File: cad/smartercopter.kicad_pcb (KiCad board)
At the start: 2 copper layers, 37.7 x 16.8 mm, 74 parts, among them P1 CONN_5, P2 CONN_01X01, P3 CONN_01X01, P4 CONN_2, P5 CONN_01X01, P6 CONN_01X01, P7 CONN_01X01, Q1 SiA910EDJ, SW1 SW_PUSH_4, U1 CC2541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

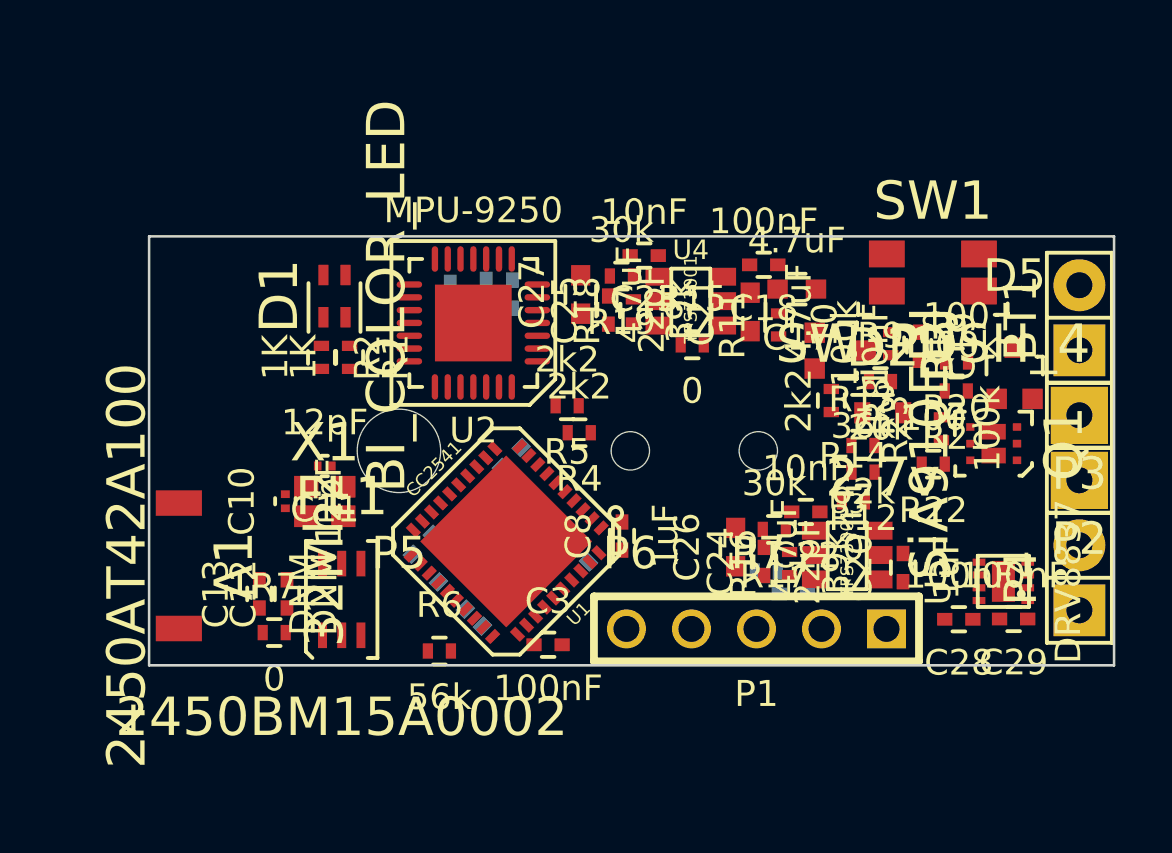
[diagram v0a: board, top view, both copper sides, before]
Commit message: everything routed
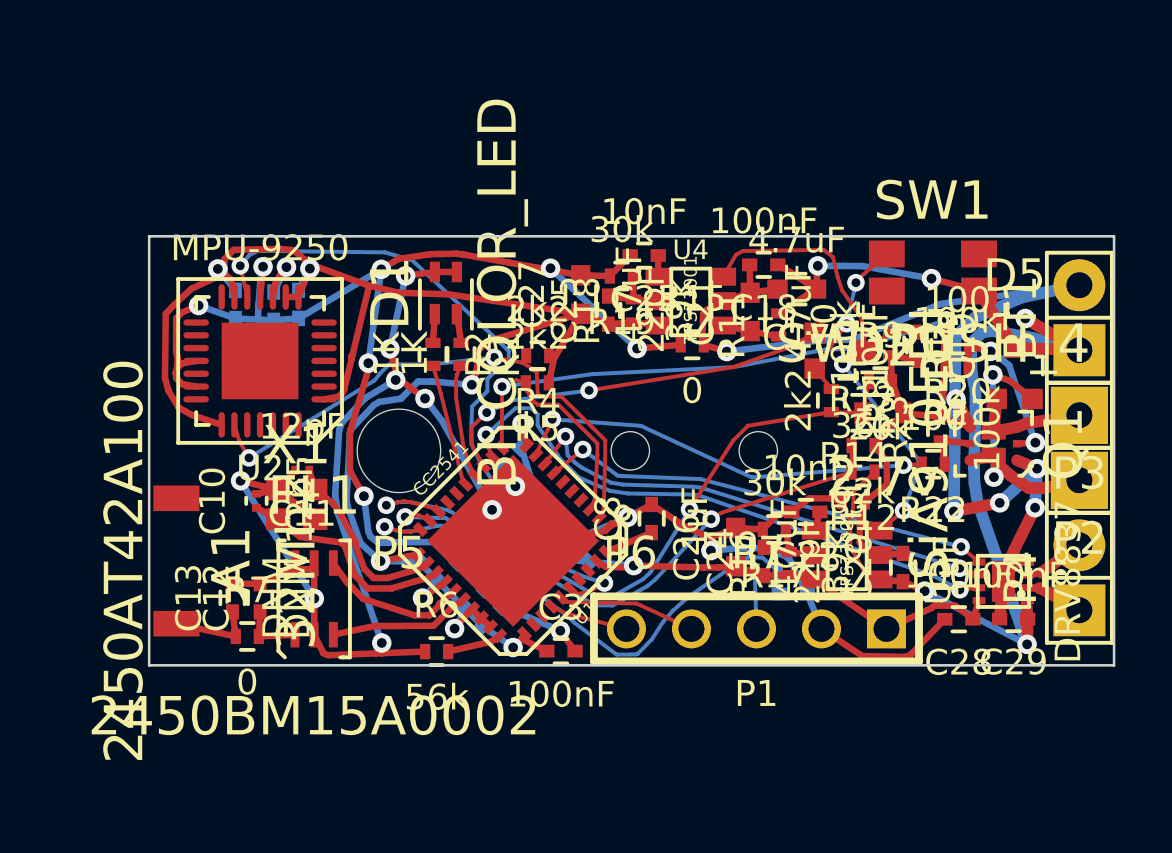
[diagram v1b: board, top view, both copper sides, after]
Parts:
- moved U2 8.46 mm to (55.7, 109.4)
- moved C15 8.40 mm to (54.7, 107.2)
- moved C16 8.36 mm to (57.2, 107.2)
- moved C14 8.32 mm to (56.2, 107.2)
- moved D1 4.36 mm to (62.9, 106.7)
- moved R2 4.36 mm to (62.4, 109.1)
- moved R1 4.36 mm to (63.5, 109.1)
- moved R4 3.42 mm to (66.5, 109.2)
- moved R5 1.47 mm to (66.5, 110.2)
- moved C8 1.35 mm to (70.9, 115.5)
- moved C10 1.13 mm to (55.5, 114.8)
- moved X1 1.10 mm to (57.1, 115.0)
- moved FL1 1.07 mm to (57.8, 118.7)
- moved R7 1.06 mm to (55.2, 120.1)
- moved C12 1.06 mm to (55.7, 118.6)
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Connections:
- U1 pad 14: Net-(U1-Pad14) -> /LED1
- U1 pad 15: Net-(U1-Pad15) -> /LED2
- U1 pad 32: /LED2 -> Net-(U1-Pad32)
- U1 pad 33: /LED1 -> Net-(U1-Pad33)
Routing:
- net DGND: track 0.00 -> 79.5 mm, vias 0 -> 11
- net VCCA: track 0.00 -> 71.7 mm, vias 0 -> 7
- net GND: track 0.00 -> 63.1 mm, vias 0 -> 6
- net AGND: track 0.00 -> 53.3 mm, vias 0 -> 8
- net +BATT: track 0.00 -> 48.2 mm, vias 0 -> 5
- net /sensors/INT: track 0.00 -> 27.1 mm, vias 0 -> 2
- net /power/BUTTON: track 0.00 -> 26.4 mm, vias 0 -> 2
- net VCC: track 0.00 -> 25.9 mm, vias 0 -> 2
- net /motor/nSLEEP: track 0.00 -> 22.9 mm, vias 0 -> 2
- net /power/BATTVOLT: track 0.00 -> 22.0 mm, vias 0 -> 2
- net /sensors/SCL: track 0.00 -> 21.6 mm, vias 0 -> 2
- net Net-(C9-Pad1): track 0.00 -> 21.1 mm, vias 0 -> 1
- net /motor/UP_ROTOR: track 0.00 -> 21.1 mm, vias 0 -> 2
- net /power/EN_REG: track 0.00 -> 20.3 mm, vias 0 -> 2
- net /motor/PH: track 0.00 -> 19.0 mm, vias 0 -> 2
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
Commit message: everything routed for sure this time
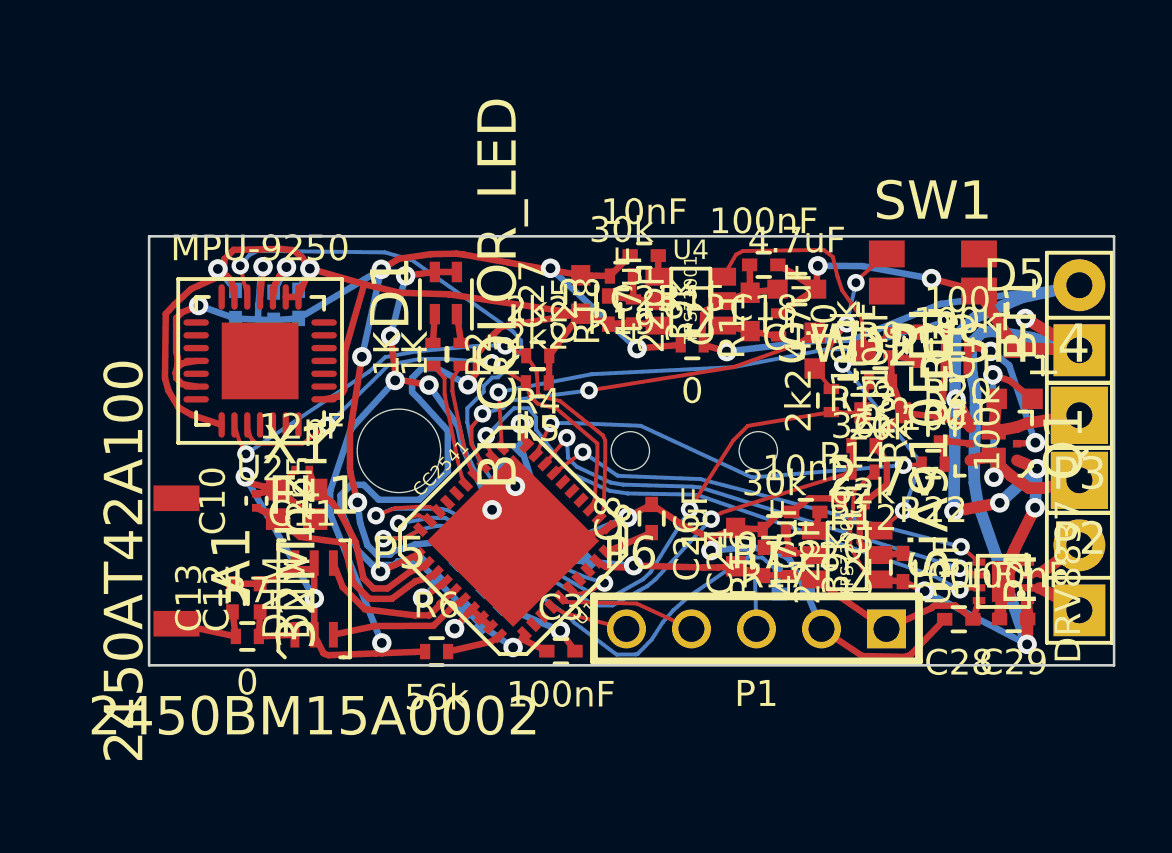
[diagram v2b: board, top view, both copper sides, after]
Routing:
- net /sensors/SDA: track 6.98 -> 19.2 mm, vias 0 -> 2
- net VCCA: track 71.7 -> 76.2 mm
- net /power/BUTTON: track 26.4 -> 27.2 mm
- net /sensors/INT: track 27.1 -> 27.9 mm
- net /power/BATTVOLT: track 22.0 -> 22.6 mm
- net /XOSC_Q1: track 7.25 -> 7.83 mm
- net /XOSC_Q2: track 8.61 -> 9.17 mm
- net DGND: track 79.5 -> 79.0 mm

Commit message: no drc errors
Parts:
- moved C22 0.50 mm to (77.0, 114.8)
- moved R15 0.33 mm to (72.4, 109.1)
- moved R17 0.27 mm to (75.8, 115.7)
- moved C14 0.08 mm to (56.2, 107.2)
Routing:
- net VCCA: track 76.2 -> 77.2 mm
- net GND: track 63.1 -> 62.4 mm, vias 6 -> 5
- net DGND: track 79.0 -> 79.5 mm
- net /sensors/INT: track 27.9 -> 27.3 mm

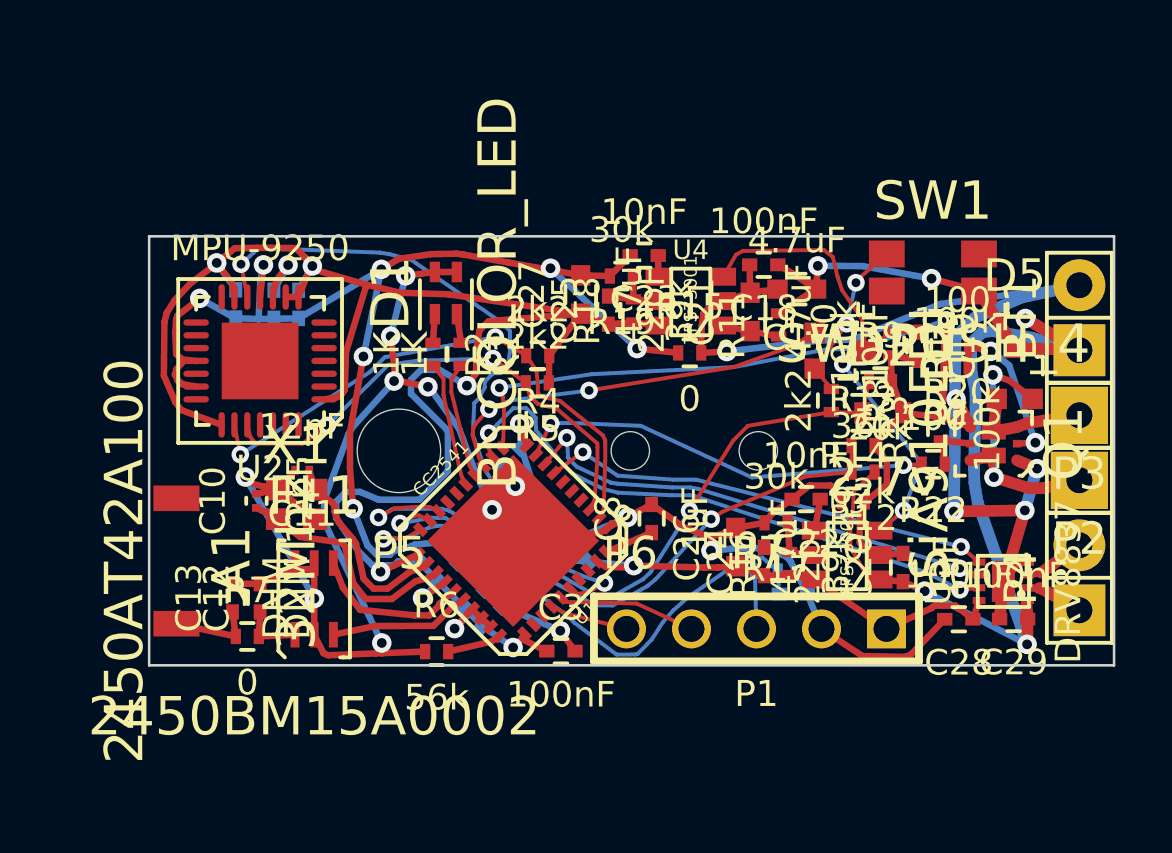
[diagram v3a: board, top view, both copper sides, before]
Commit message: added some ground planes
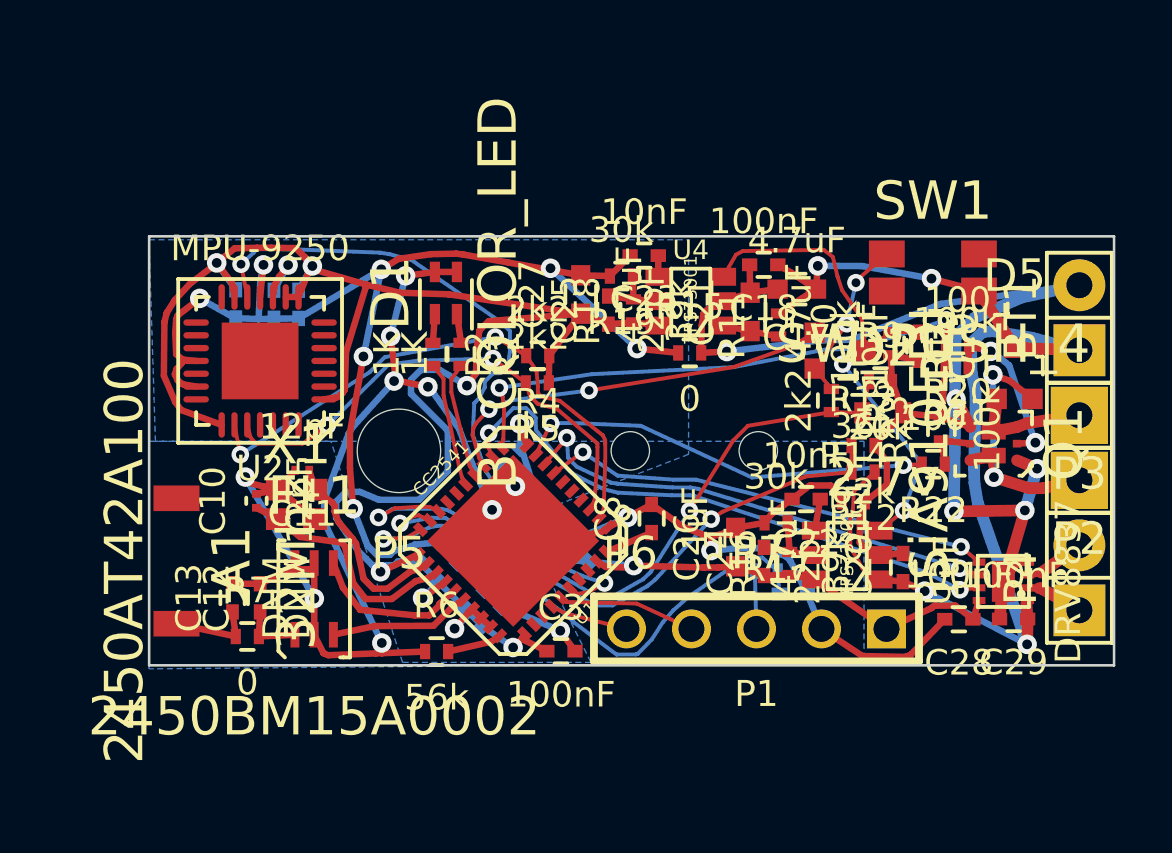
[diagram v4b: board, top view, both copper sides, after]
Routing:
- net +BATT: track 48.2 -> 45.7 mm, vias 5 -> 4
- added copper zone on B.Cu, net AGND
- added copper zone on B.Cu, net DGND

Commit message: more power planes
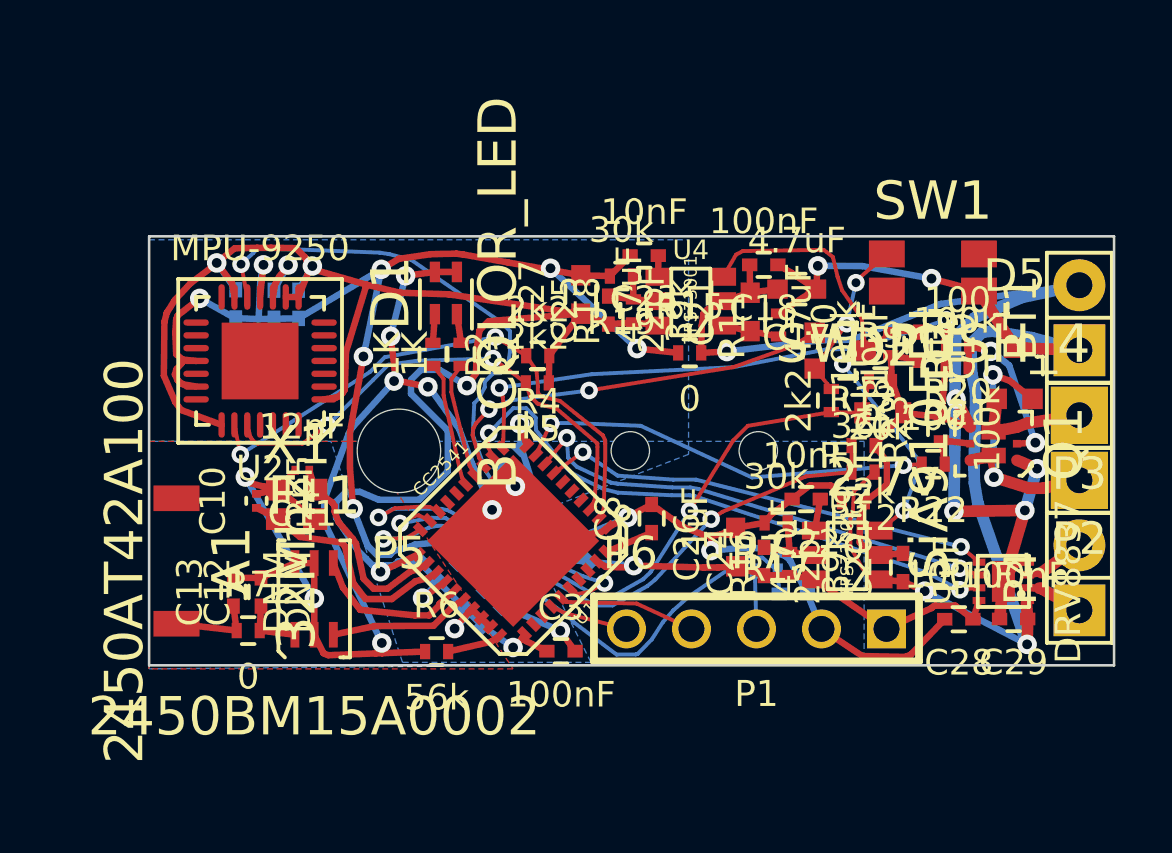
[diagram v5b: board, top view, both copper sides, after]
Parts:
- moved C12 0.23 mm to (55.7, 118.4)
- moved C13 0.23 mm to (54.6, 118.4)
- moved R7 0.23 mm to (55.2, 119.9)
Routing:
- added copper zone on F.Cu, net DGND

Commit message: double checking qfn-40 footprint
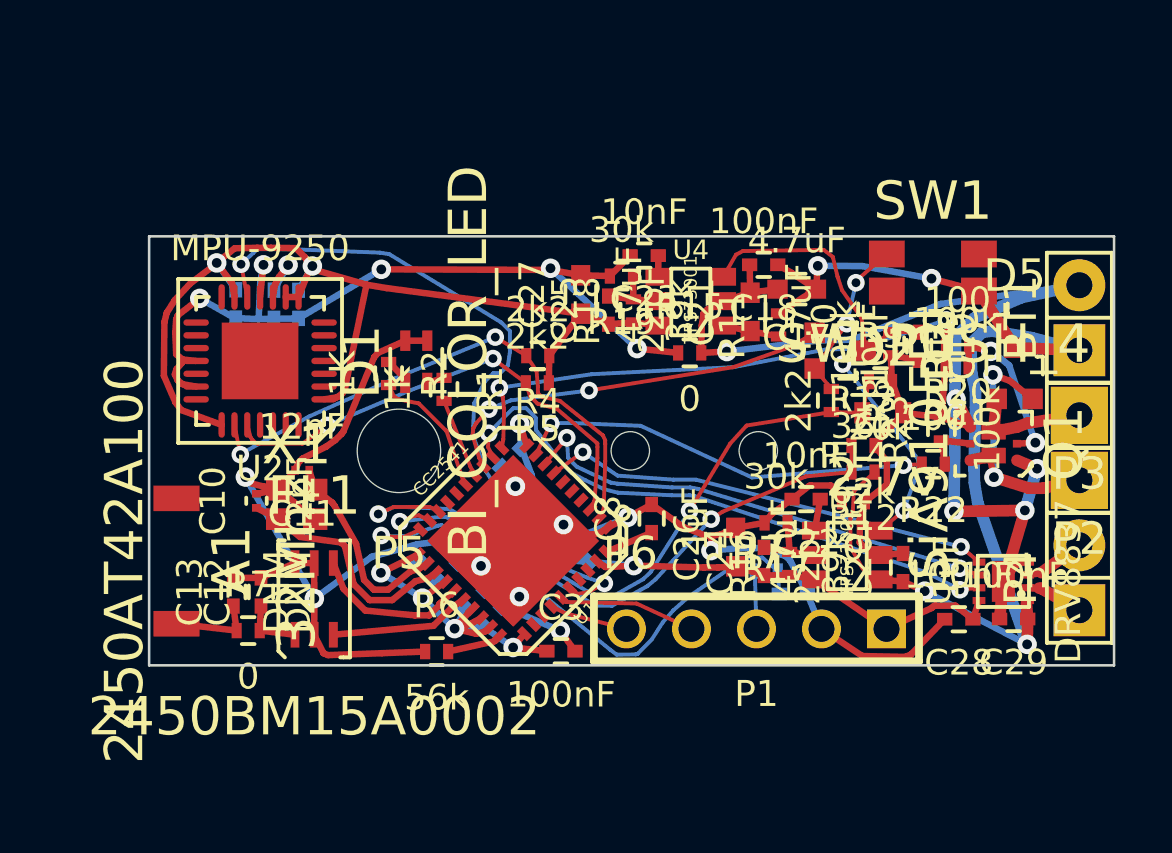
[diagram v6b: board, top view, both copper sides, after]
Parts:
- moved D1 2.93 mm to (61.8, 109.4)
- moved R2 1.88 mm to (60.7, 109.9)
- moved R1 1.52 mm to (62.8, 110.5)
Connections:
- C3 pad 1: VCCA -> VCC
- C3 pad 2: AGND -> DGND
- C4 pad 1: VCCA -> VCC
- C4 pad 2: AGND -> DGND
- C5 pad 1: VCCA -> VCC
- C5 pad 2: AGND -> DGND
- C6 pad 1: VCCA -> VCC
- C6 pad 2: AGND -> DGND
- C7 pad 1: VCCA -> VCC
- C7 pad 2: AGND -> DGND
- U1 pad 21: VCCA -> VCC
- U1 pad 24: VCCA -> VCC
- U1 pad 27: VCCA -> VCC
- U1 pad 28: VCCA -> VCC
- U1 pad 29: VCCA -> VCC
- U1 pad 31: VCCA -> VCC
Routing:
- net VCCA: track 77.2 -> 40.6 mm, vias 7 -> 2
- net AGND: track 54.1 -> 32.8 mm, vias 8 -> 5
- net VCC: track 25.9 -> 41.4 mm, vias 2 -> 6
- net DGND: track 79.2 -> 81.1 mm, vias 11 -> 9
- net /LED1: track 4.53 -> 3.15 mm
- removed copper zone on B.Cu, net AGND
- removed copper zone on B.Cu, net DGND
- removed copper zone on F.Cu, net DGND

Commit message: changed cc2451 footprint center pad
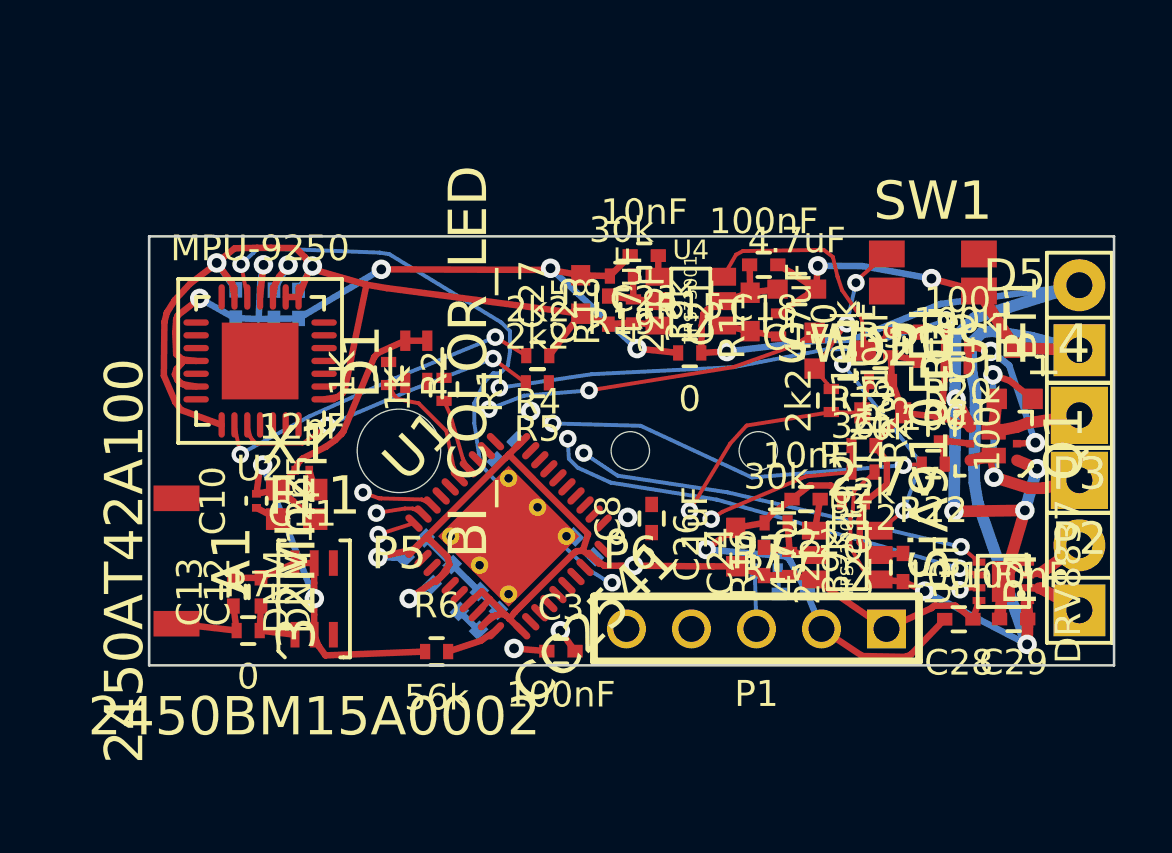
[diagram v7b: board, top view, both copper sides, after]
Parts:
- U1: footprint SMD_Packages:LFCSP-40-1EP -> hlib:VQFN-40
- moved C5 0.55 mm to (61.7, 116.7)
- moved C2 0.32 mm to (65.3, 112.9)
- moved C1 0.31 mm to (68.3, 116.6)
- moved C4 0.26 mm to (62.8, 117.7)
- moved U1 0.26 mm to (65.4, 116.2)
- moved C6 0.25 mm to (63.8, 118.8)
- moved C7 0.22 mm to (64.6, 119.5)
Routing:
- net DGND: track 81.1 -> 52.8 mm, vias 9 -> 4
- net /motor/nSLEEP: track 22.8 -> 0.75 mm, vias 2 -> 1
- net Net-(C9-Pad1): track 21.4 -> 2.36 mm
- net /power/BUTTON: track 27.1 -> 12.6 mm
- net /power/BATTVOLT: track 22.6 -> 8.79 mm
- net /XOSC_Q2: track 9.24 -> 0.95 mm
- net /sensors/SCL: track 21.5 -> 13.6 mm
- net /XOSC_Q1: track 7.89 -> 0.79 mm
- net /sensors/SDA: track 18.9 -> 12.4 mm
- net /RF_P: track 6.19 -> 0.00 mm
- net /RF_N: track 5.49 -> 0.00 mm
- net /DD: track 5.39 -> 0.00 mm
- net VCC: track 41.4 -> 46.2 mm, vias 6 -> 4
- net /DC: track 3.06 -> 0.00 mm
- net /power/EN: track 15.7 -> 13.2 mm
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
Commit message: all routed
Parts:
- moved C1 0.62 mm to (68.9, 116.6)
- moved C8 0.60 mm to (70.4, 115.6), turned to 135 degrees
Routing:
- net DGND: track 52.8 -> 82.5 mm, vias 4 -> 6
- net /motor/nSLEEP: track 0.75 -> 22.1 mm, vias 1 -> 2
- net Net-(C9-Pad1): track 2.36 -> 22.1 mm
- net /power/BATTVOLT: track 8.79 -> 24.2 mm
- net /power/BUTTON: track 12.6 -> 28.0 mm
- net /sensors/SCL: track 13.6 -> 21.4 mm
- net /XOSC_Q2: track 0.95 -> 8.43 mm
- net VCC: track 46.2 -> 52.8 mm, vias 4 -> 5
- net /sensors/SDA: track 12.4 -> 18.7 mm
- net /XOSC_Q1: track 0.79 -> 7.06 mm
- net /RF_P: track 0.00 -> 6.02 mm
- net /DD: track 0.00 -> 5.51 mm
- net /RF_N: track 0.00 -> 5.47 mm
- net /DC: track 0.00 -> 3.20 mm
- net /power/EN: track 13.2 -> 16.1 mm
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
